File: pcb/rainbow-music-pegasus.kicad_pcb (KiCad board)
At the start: 2 copper layers, 151 x 31 mm, 112 parts, among them J1 USB_B_Micro, J2 Conn_02x03_Odd_Even, J3 B2B-PH-K-S, Q1 DMG3415U, SW1 SW_SPDT, SW2 EVQQ2, U1 ESP32-C3-MINI-1, U2 OPA2322, U3 TLV75533PDBV, U4 MCP73831-2-OT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

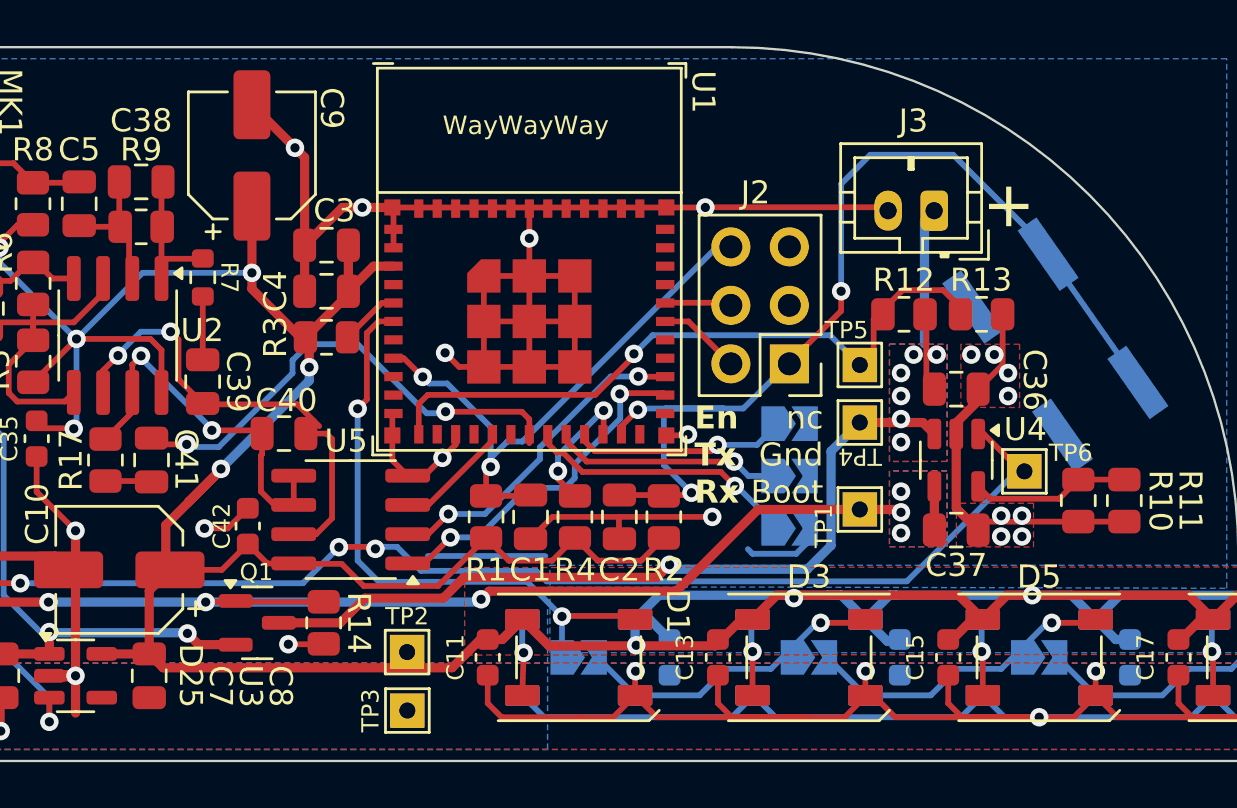
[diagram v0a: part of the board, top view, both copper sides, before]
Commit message: Move TP6 to the DP_Wiper, add TP7 to DP_A and TP8 to MIC feed
Also fixed the size of all Touchpoints to allow for soldering thru-hole pins
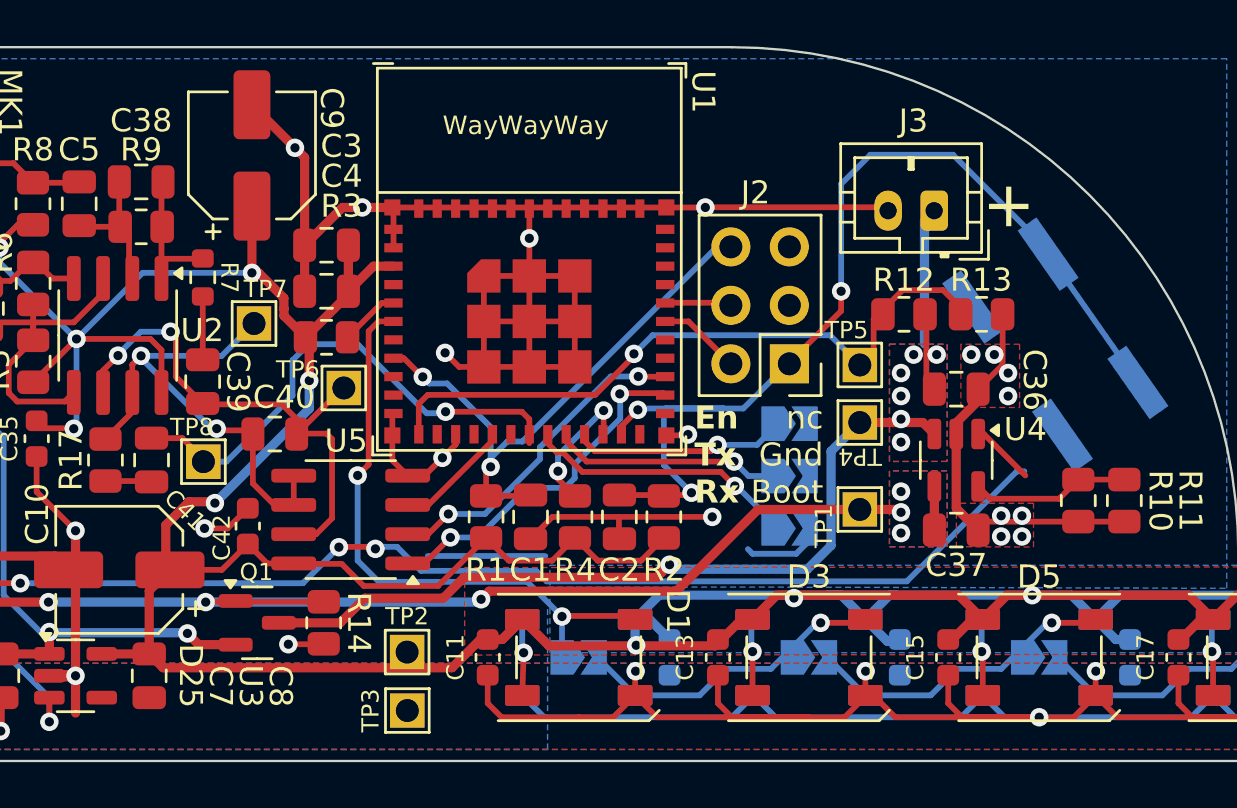
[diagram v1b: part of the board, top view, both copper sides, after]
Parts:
- added TP7: TestPoint, TestPoint:TestPoint_THTPad_1.5x1.5mm_Drill0.7mm, F.Cu at (101.7, 86.1)
- added TP8: TestPoint, TestPoint:TestPoint_THTPad_1.5x1.5mm_Drill0.7mm, F.Cu at (99.5, 92.1)
- moved TP6 29.8 mm to (105.6, 88.9)
- moved C40 0.40 mm to (102.6, 90.9)
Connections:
- TP6 pad 1: Net-(U4-STAT) -> /DP_B
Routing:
- net /DP_W: track 16.9 -> 22.0 mm
- net /DP_B: track 20.4 -> 23.2 mm
- net /Mic_Signal: track 20.9 -> 22.4 mm, vias 2 -> 1
- net +3.3V: track 398.3 -> 397.1 mm

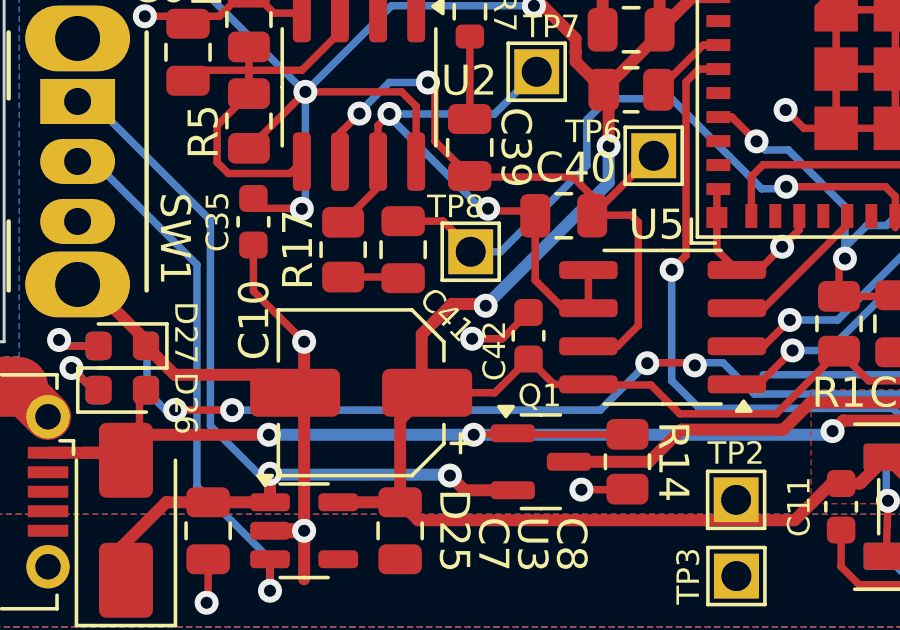
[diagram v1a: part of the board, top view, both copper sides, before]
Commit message: Upgrade to KiCAD 10
Also resized Altivo to better fit in available back silkscreen area
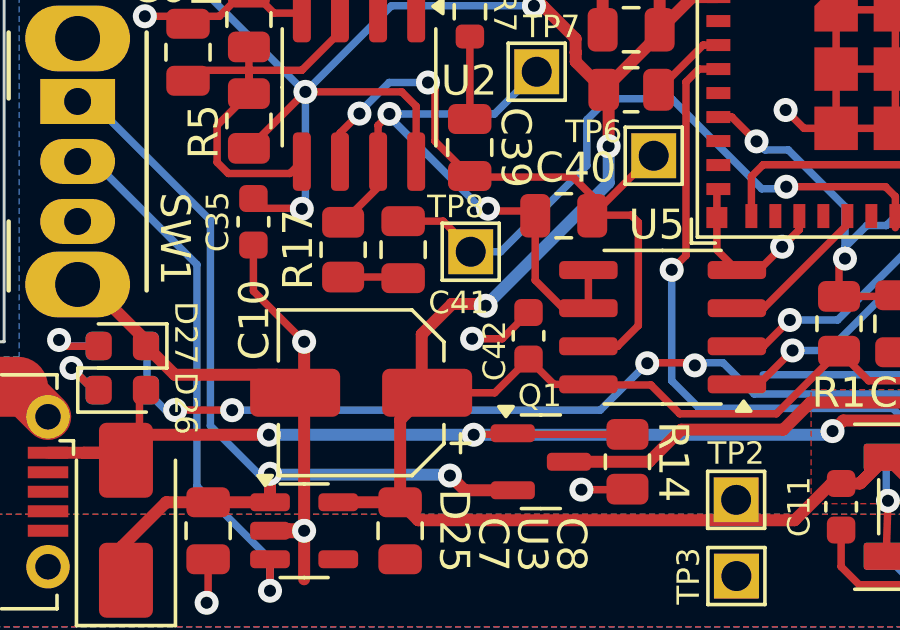
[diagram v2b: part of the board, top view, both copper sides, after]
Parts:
- moved G*** 1.46 mm to (97.2, 92.5)
